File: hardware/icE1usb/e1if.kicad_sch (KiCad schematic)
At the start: 25 parts, among them J5 NT/TE, U11 IP4220CZ6, U12 IP4220CZ6

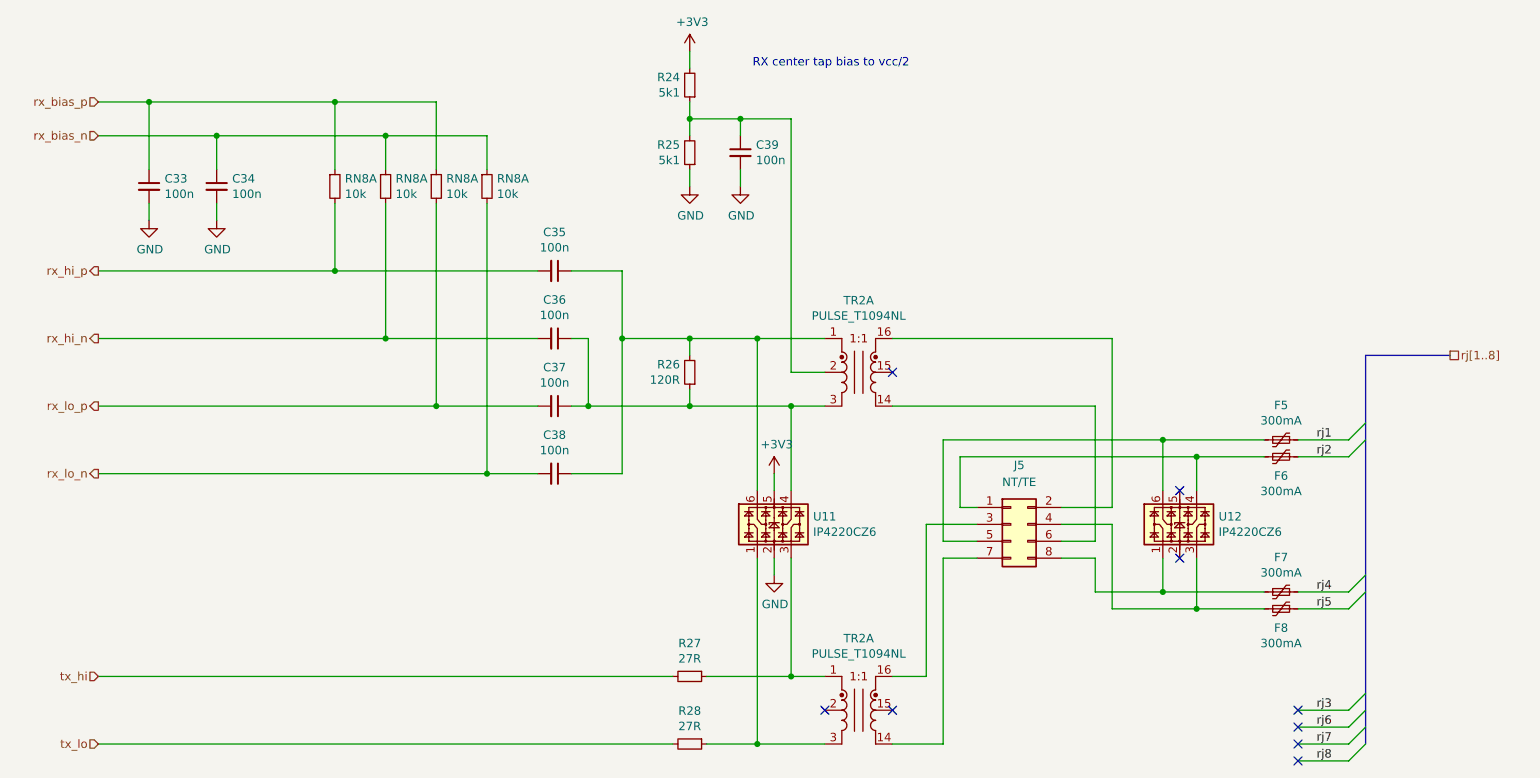
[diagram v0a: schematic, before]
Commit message: hardware/icE1usb: Kicad file minor updates
* Renumber schematic pages
* Update the info cards with new data and r1.1

Signed-off-by: Sylvain Munaut <tnt@246tNt.com>
Change-Id: Ie5f3aa59e97fe46be9c857cf91ac4ff4ef72384e
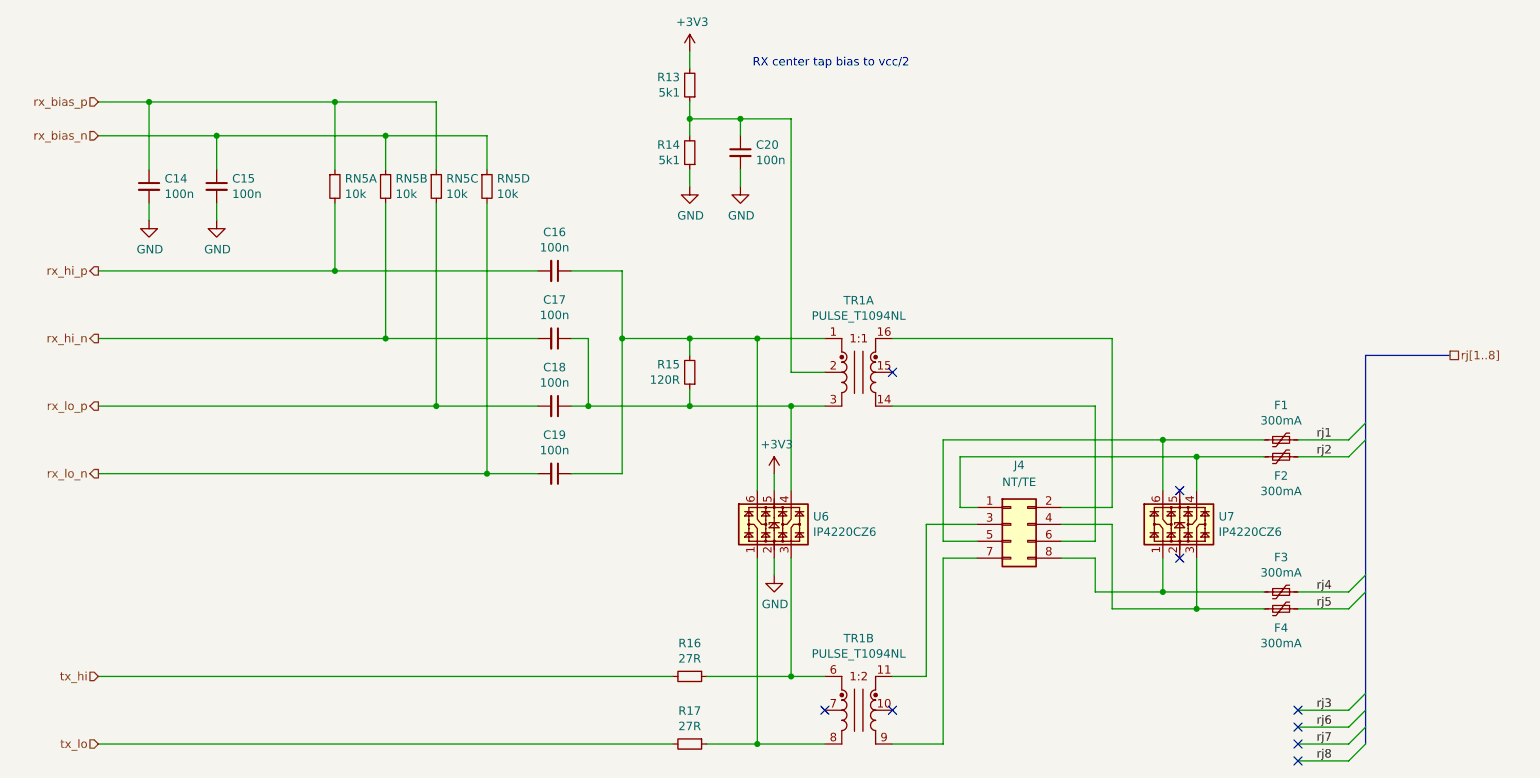
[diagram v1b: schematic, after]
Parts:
- renumbered C33 to C14, C34 to C15, C35 to C16, C36 to C17, C37 to C18, C38 to C19, C39 to C20, F5 to F1, F6 to F2, F7 to F3, F8 to F4, J5 to J4, R24 to R13, R25 to R14, R26 to R15, R27 to R16, R28 to R17, RN8 to RN5, TR2 to TR1, U11 to U6, U12 to U7
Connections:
- net rx_bias_n: now also RN5.2, RN5.4; no longer RN5.1, RN5.1
- net rx_bias_p: now also RN5.3; no longer RN5.1
- net rx_hi_n: now also RN5.7; no longer RN5.8
- net rx_lo_n: now also RN5.5; no longer RN5.8
- net rx_lo_p: now also RN5.6; no longer RN5.8
- net at R16.1, U6.3: now also TR1.6; no longer TR1.1
- net at J4.7 (Pin_7): now also TR1.9; no longer TR1.14
- net at J4.3 (Pin_3): now also TR1.11; no longer TR1.16
- net at R17.1, U6.1: now also TR1.8; no longer TR1.3
